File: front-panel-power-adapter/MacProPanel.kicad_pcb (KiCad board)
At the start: 2 copper layers, 55.9 x 36.8 mm, 5 parts, among them P3 CONN_02X04, P4 CONN_02X05, P7 CONN_02X12, P8 CONN_02X12

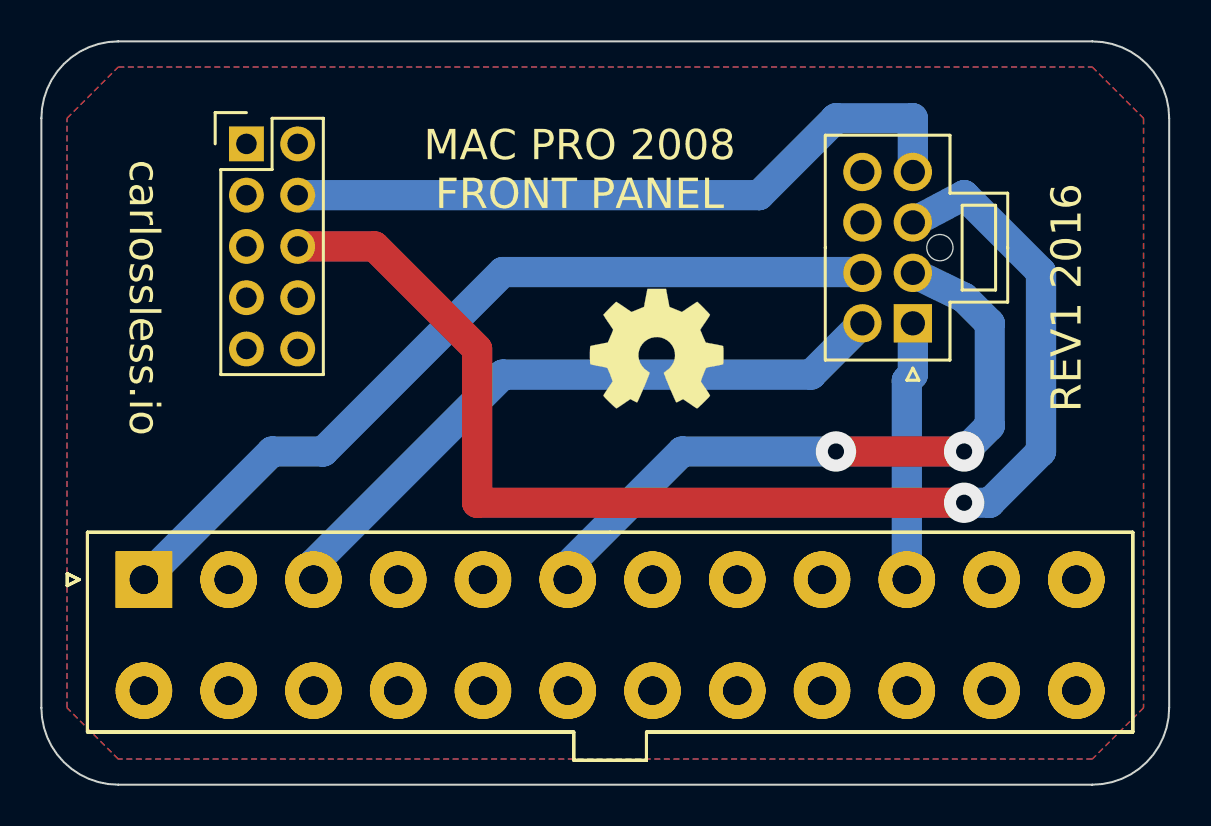
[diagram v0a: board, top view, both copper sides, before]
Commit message: Fron Panel Nanofit connector exchanged with microfit3
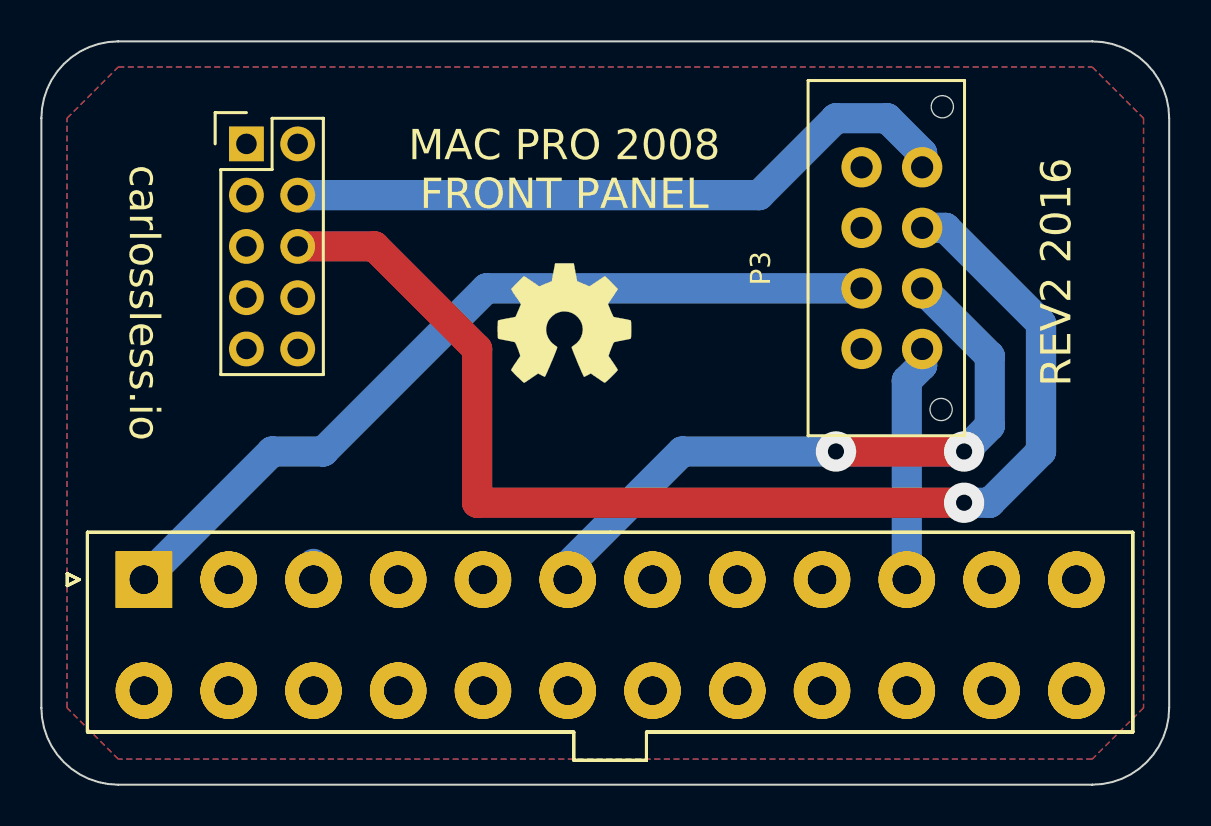
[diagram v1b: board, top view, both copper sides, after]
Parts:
- P3: footprint Connectors_Molex:Molex_NanoFit_2x04x2.50mm_Straight -> Connectors_Molex:Molex_Microfit3_Header_02x04_Straight_43045-0828
- moved REF*** 4.75 mm to (193.5, 76.2)
- moved P3 2.84 mm to (208.3, 77.5), turned to 270 degrees
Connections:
- P3 pad 1: ATX10_12V -> GND
- P3 pad 2: ATX06_5V -> ATX01_3.3V
- P3 pad 3: MB_PW+ -> Net-(P3-Pad3)
- P3 pad 4: MB_MSG- -> Net-(P3-Pad4)
- P3 pad 5: GND -> ATX10_12V
- P3 pad 6: ATX01_3.3V -> ATX06_5V
- P3 pad 7: Net-(P3-Pad7) -> MB_PW+
- P3 pad 8: Net-(P3-Pad8) -> MB_MSG-
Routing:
- net GND: track 32.9 -> 0.78 mm
- net MB_PW+: track 64.8 -> 61.8 mm
- net ATX06_5V: track 34.2 -> 32.7 mm
- net ATX10_12V: track 12.8 -> 11.7 mm
- net MB_MSG-: track 34.7 -> 33.9 mm
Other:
- board text added: "REV2 2016"
- board text removed: "REV1 2016"
